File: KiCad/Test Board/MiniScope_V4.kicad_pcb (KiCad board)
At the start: 6 copper layers, 30.5 x 43.8 mm, 45 parts, among them J1 Conn_01x05, J10 Conn_01x01, J11 Conn_01x01, J12 Conn_01x01, J13 Conn_01x01, J14 Conn_01x01, J15 Conn_01x01, J22 Conn_01x20, J24 Conn_01x14, J3 Conn_01x01, J4 Conn_01x01, J8 0475710001, U1 TPS62402-Q1, U2 MAX13030EETE+, U3 ATSAME70N21A-CN, U4 TSOP57438TT1, Y1 ABM8G-12.000MHZ-4Y-T3

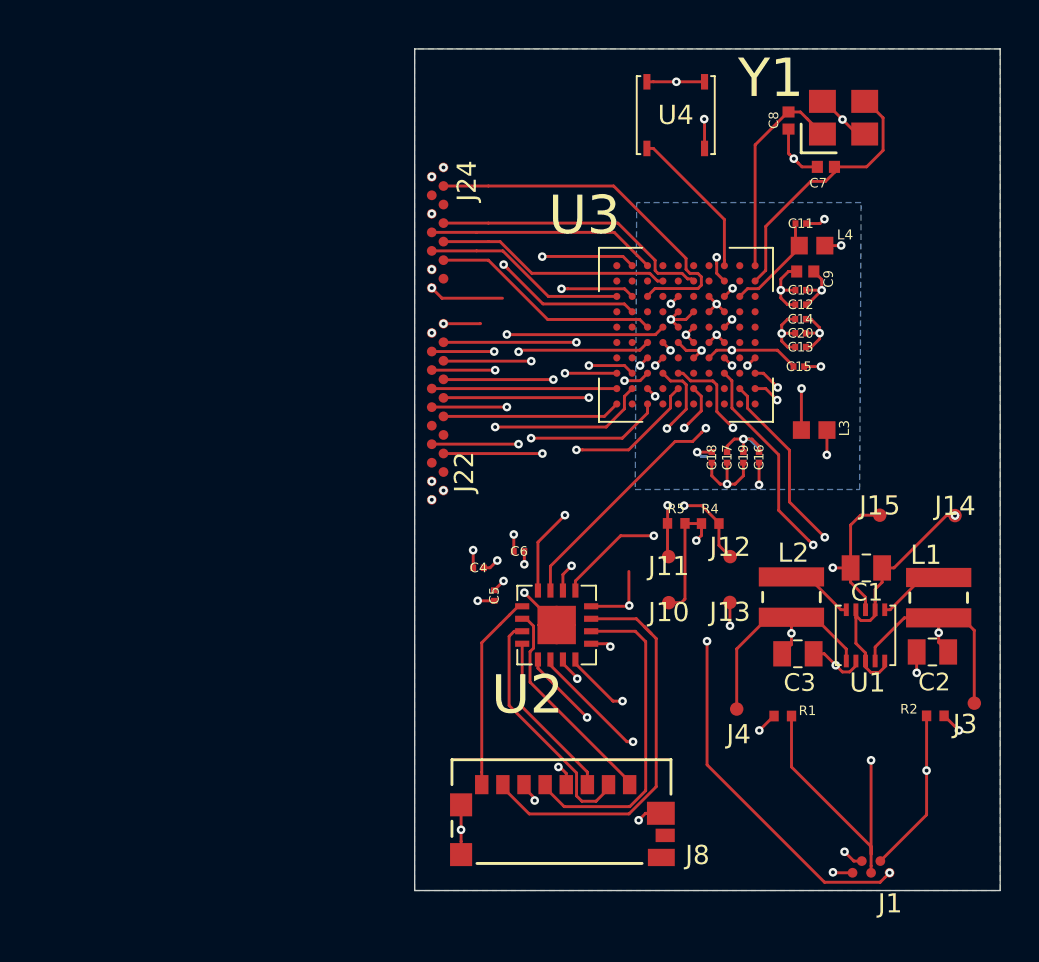
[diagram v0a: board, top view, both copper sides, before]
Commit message: Data Acquisition Software
1. Data Acquisition software written
2. Test Board: Changed I2C resistors to pull-up. Reroute the 14-pin flexPC so it fits the Python480 board
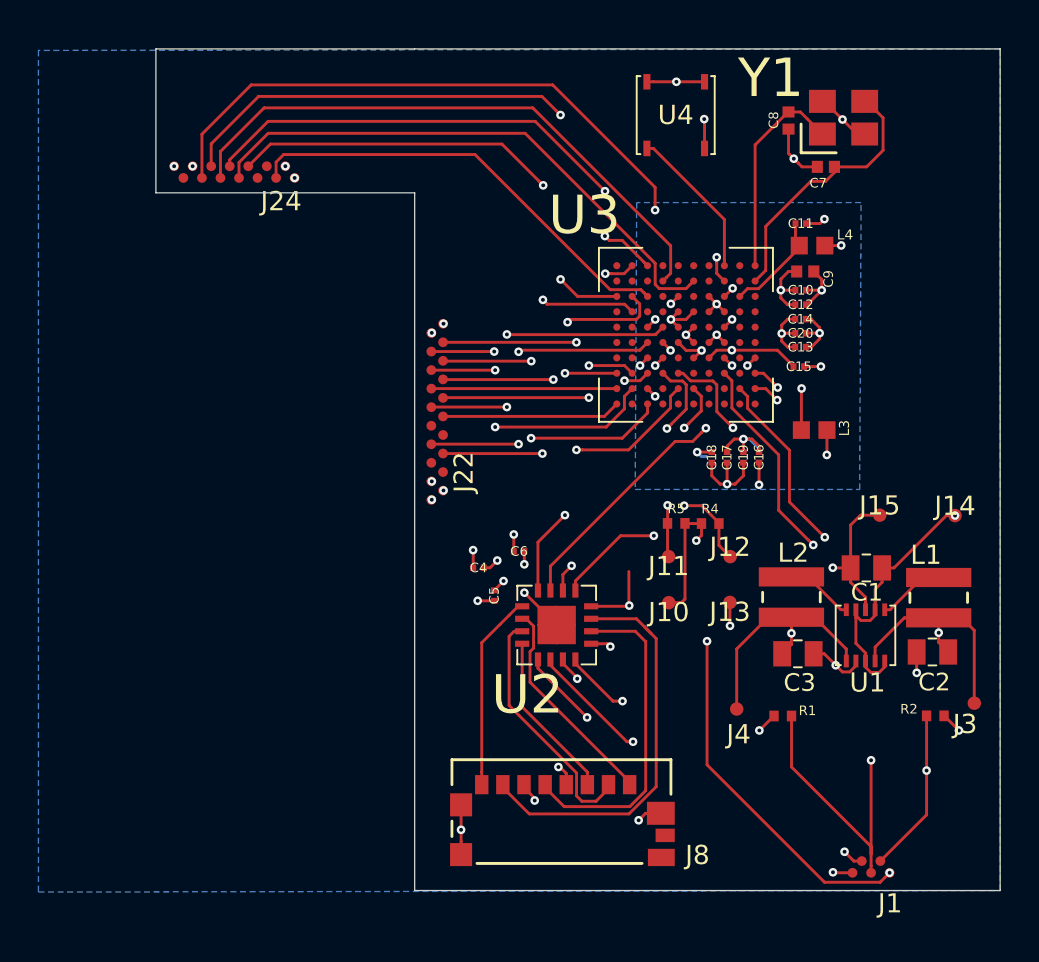
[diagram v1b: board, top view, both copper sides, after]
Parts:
- moved J24 14.8 mm to (114.5, 95.6), turned to 0 degrees
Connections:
- R1 pad 2: Earth -> +1V8
- R2 pad 2: Earth -> +1V8
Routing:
- net /CMOS Imaging Sensor Connectors/MOSI: track 12.1 -> 36.6 mm, vias 0 -> 2
- net /CMOS Imaging Sensor Connectors/MISO: track 10.6 -> 32.6 mm, vias 0 -> 2
- net +BATT: track 57.8 -> 77.5 mm
- net /CMOS Imaging Sensor Connectors/MONITOR0: track 12.3 -> 30.7 mm
- net /CMOS Imaging Sensor Connectors/TRIGGER0: track 12.0 -> 27.4 mm, vias 0 -> 2
- net /CMOS Imaging Sensor Connectors/SCK: track 12.5 -> 27.6 mm
- net /CMOS Imaging Sensor Connectors/RESET_N: track 14.6 -> 29.3 mm
- net /CMOS Imaging Sensor Connectors/SS_N: track 19.2 -> 23.4 mm
- net Earth: track 61.8 -> 57.7 mm, vias 31 -> 29
- net /CMOS Imaging Sensor Connectors/LINE_VALID: track 20.3 -> 17.4 mm
- net +1V8: track 33.4 -> 35.6 mm, vias 14 -> 16
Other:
- board size 30.5 x 43.8 mm -> 44 x 43.8 mm
